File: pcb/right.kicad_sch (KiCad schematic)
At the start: 73 parts, among them J2 AudioJack3, SW22 Y, SW23 U, SW24 I, SW25 O, SW26 P, SW27 BS, SW28 H, SW29 J, SW30 K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

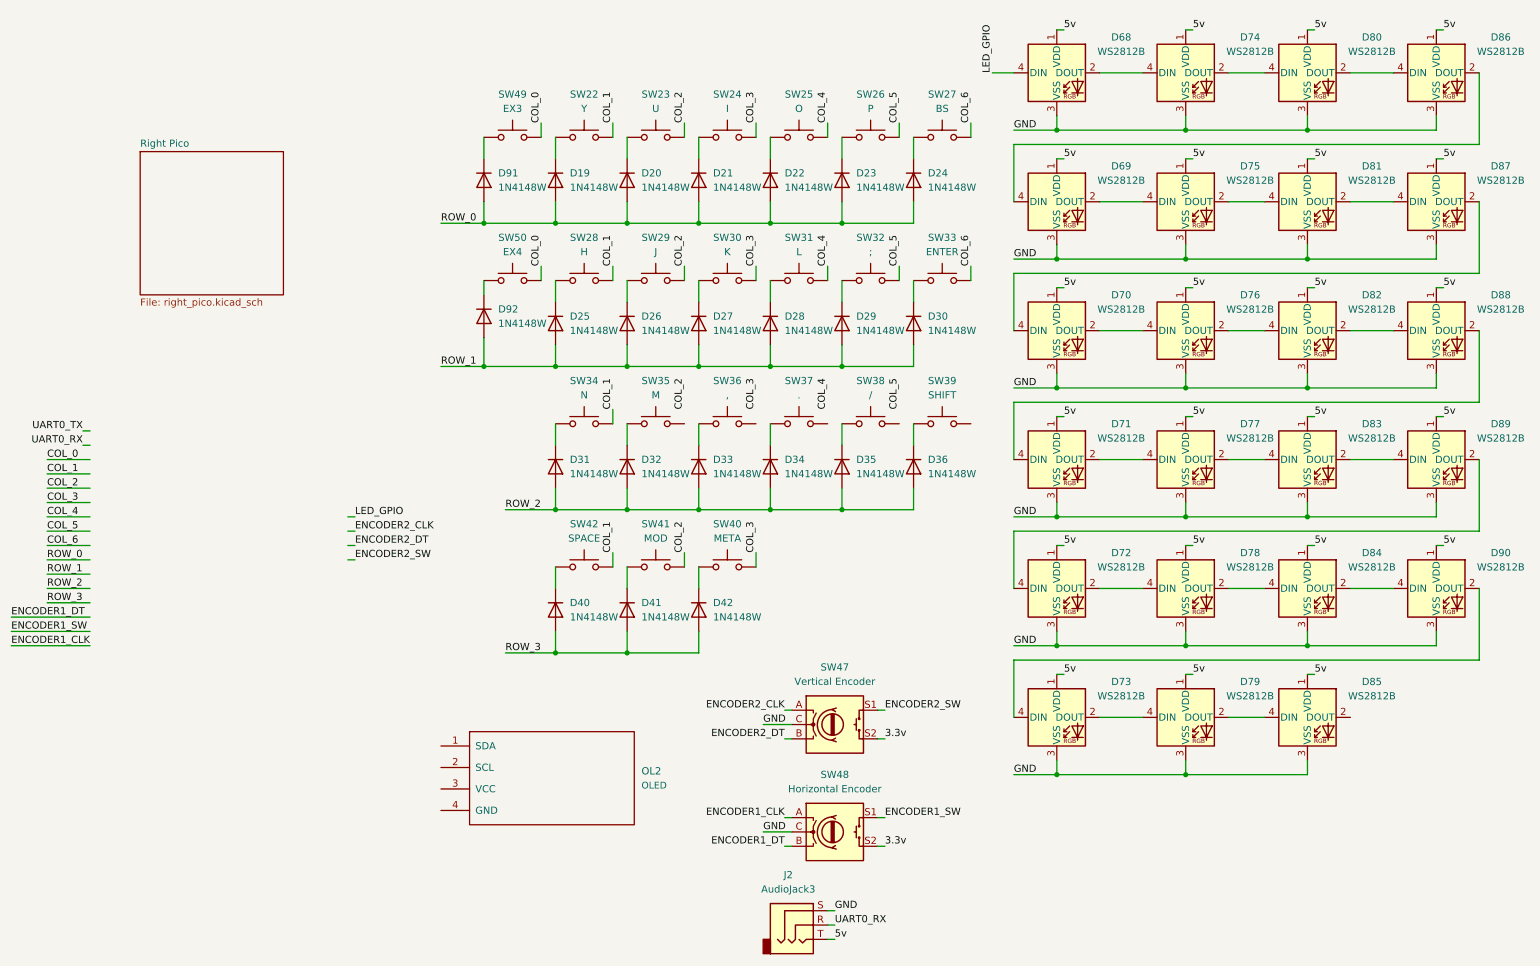
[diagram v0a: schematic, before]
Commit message: Rework edgecuts and change to waveshare rp2040 zero
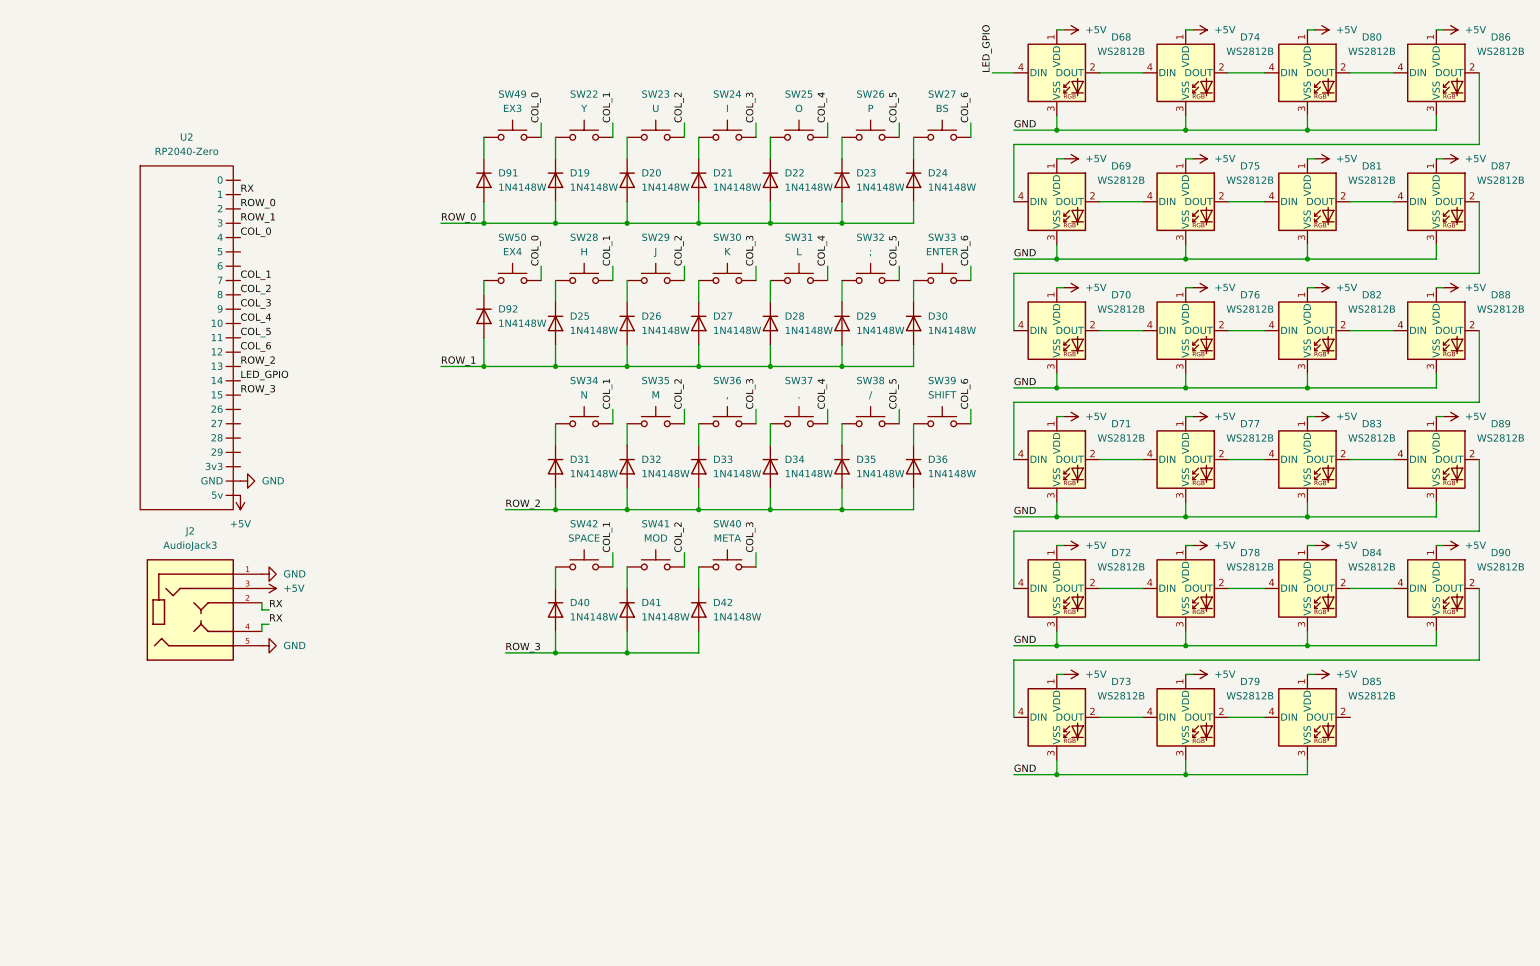
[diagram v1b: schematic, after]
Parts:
- removed J2: AudioJack3, audio-jacks:PJ-399B-6A, symbol Connector_Audio:AudioJack3
- removed OL2: OLED, oled:SSD1306-0.91-OLED-4pin-128x32, symbol kbd:OLED
- removed SW47: Vertical Encoder, encoders:PEC12R-4220F-20024, symbol Device:RotaryEncoder_Switch
- removed SW48: Horizontal Encoder, encoders:PEC12R-2120F-S0012, symbol Device:RotaryEncoder_Switch
- added J2: AudioJack3, trs-jack:CUI_SJ-3501-SMT-TR, symbol trsJack:SJ-3501-SMT-TR
- added U2: RP2040-Zero, RP2040-Zero:RP2040-Zero, symbol RP2040-Zero:RP2040-Zero
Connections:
- net COL_0: now also U2.4
- net COL_1: now also U2.7
- net COL_2: now also SW35.2, U2.8
- net COL_3: now also SW36.2, U2.9
- net COL_4: now also SW37.2, U2.10
- net COL_5: now also SW38.2, U2.11
- net COL_6: now also SW39.2, U2.12
- net GND: now also J2.1, J2.5, U2.GND
- net LED_GPIO: now also U2.14
- net ROW_0: now also U2.2
- net ROW_1: now also U2.3
- net ROW_2: now also U2.13
- net ROW_3: now also U2.15
- net 5v renamed +5V
- net +5V: now also J2.3, U2.5v
- new net RX: J2.2, J2.4, U2.1
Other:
- removed sheet Right Pico
